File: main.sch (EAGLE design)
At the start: 23 parts, among them IC1 SN754410, IC2 7805T, T1 BP103, T2 BP103, T3 BP103

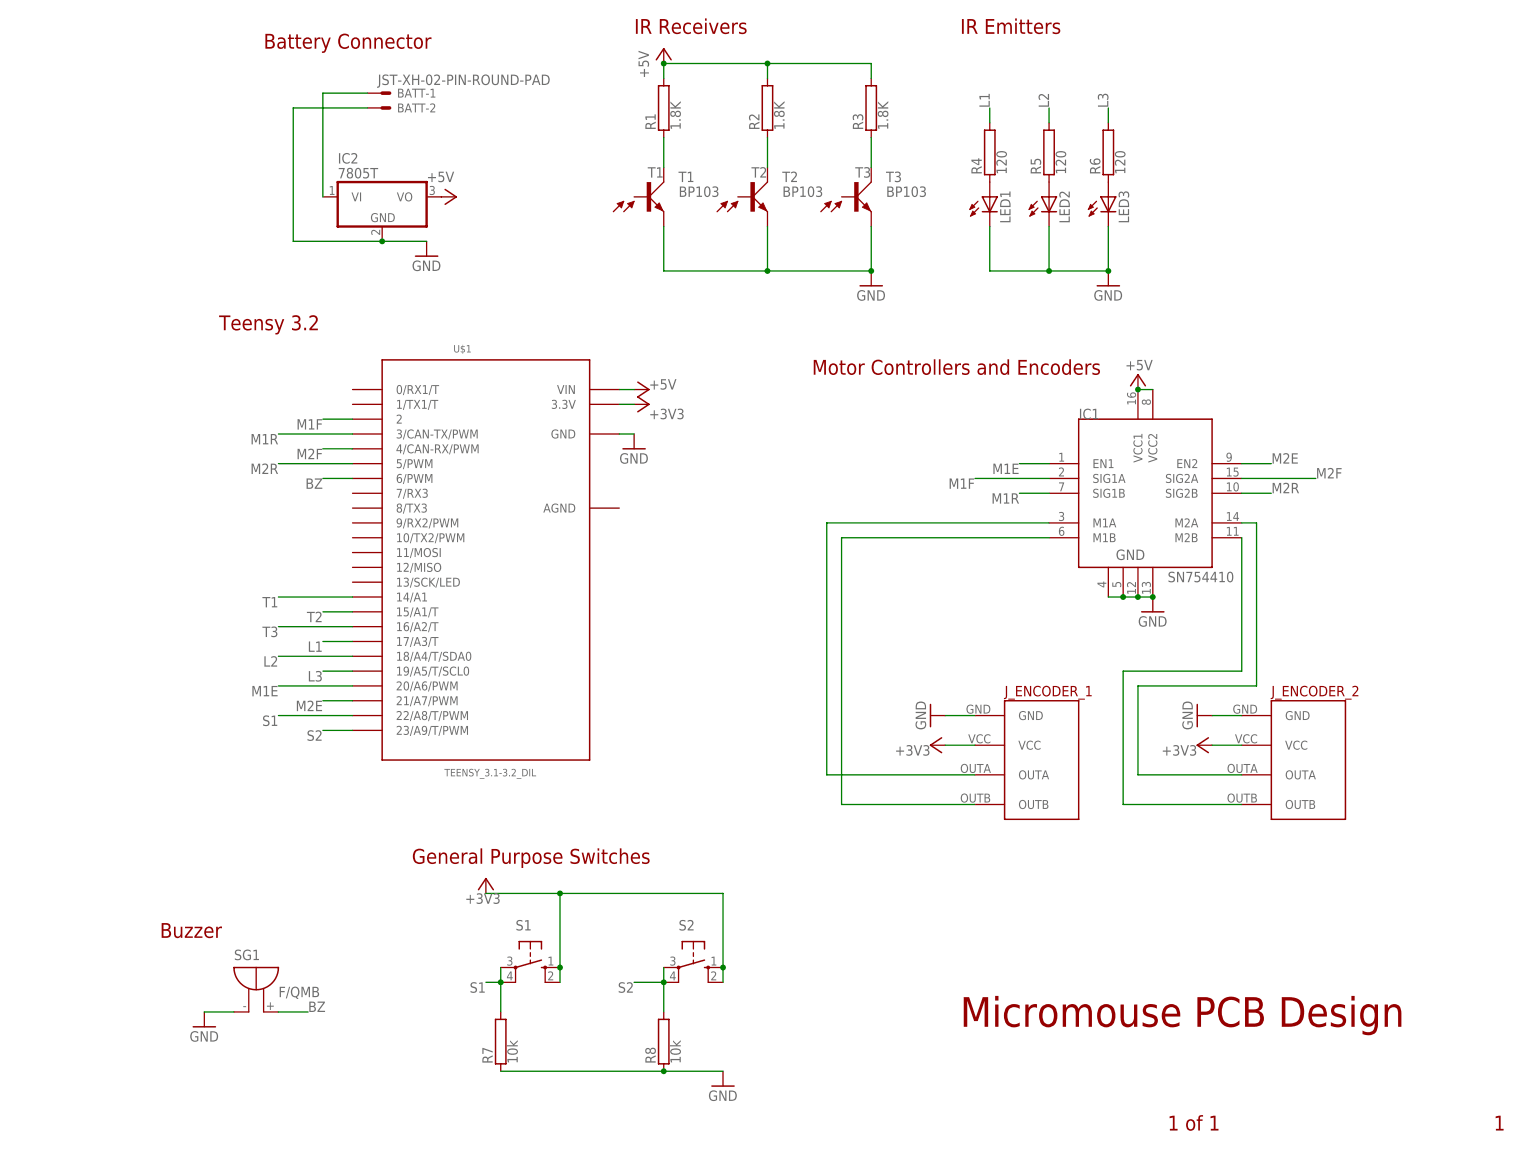
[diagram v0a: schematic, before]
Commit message: Added fourth LED/Emitter Combo and rerouted nets
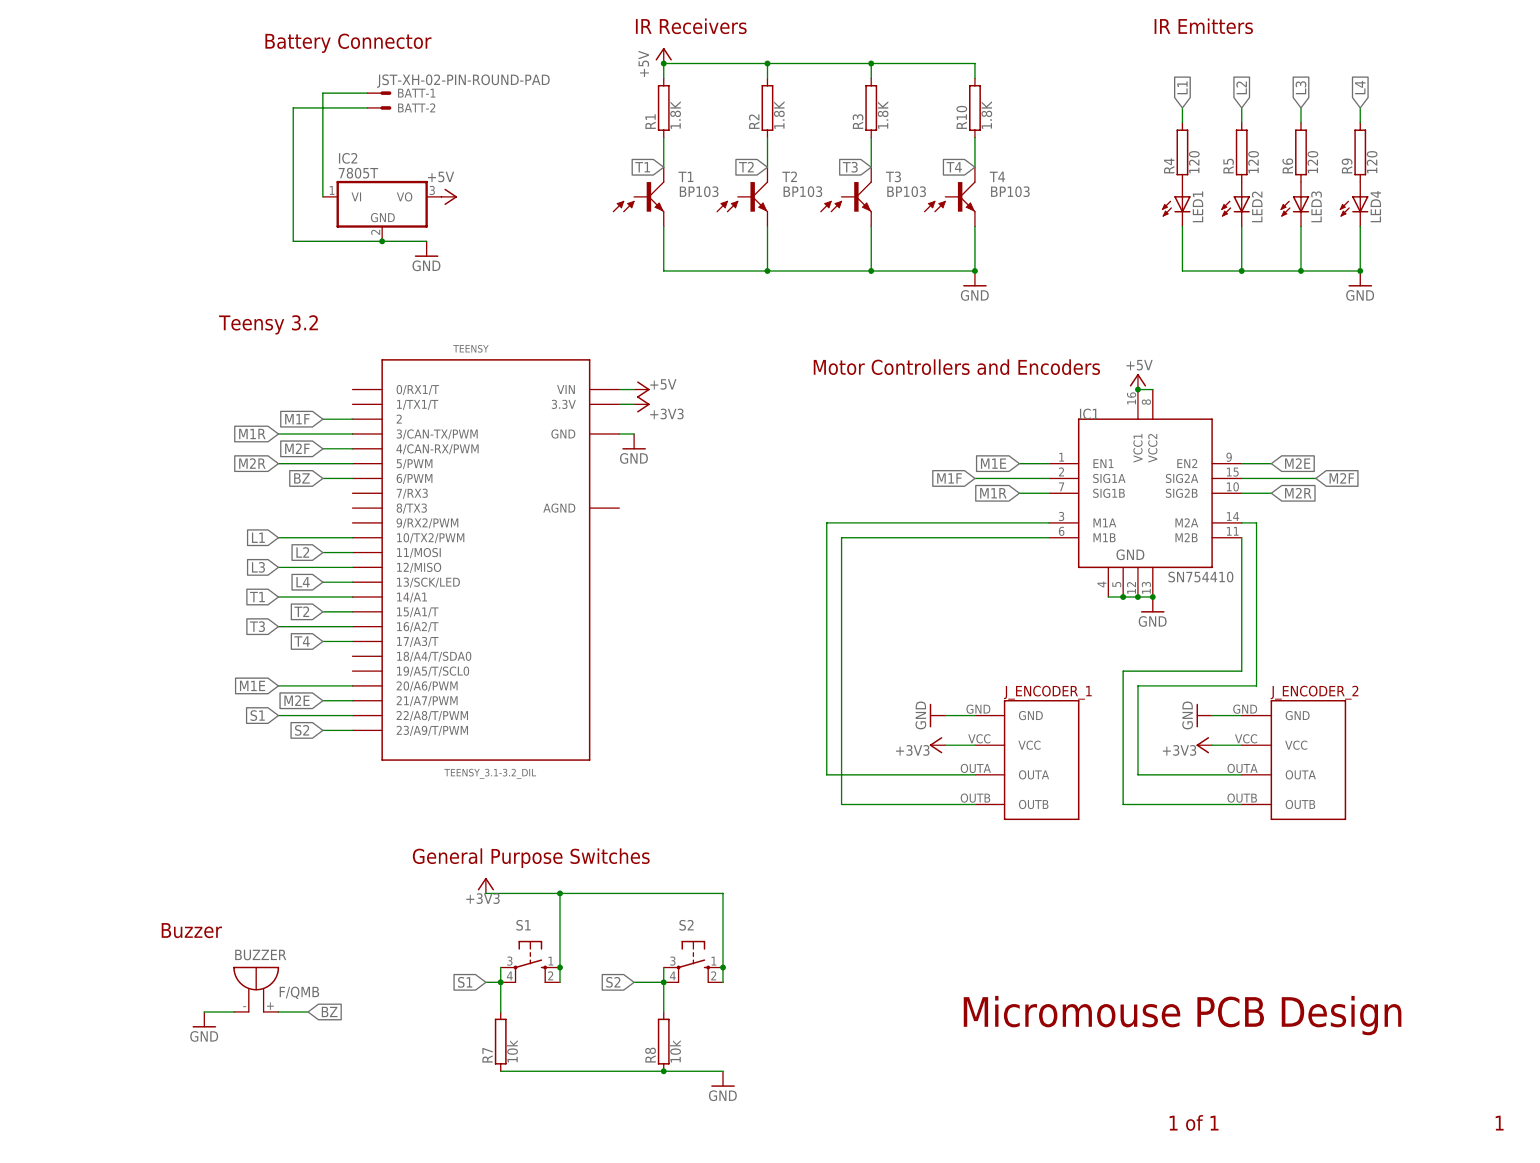
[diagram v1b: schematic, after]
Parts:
- added LED4: (no value), led:LED3MM
- added R10: 1.8K, resistor-power:RRS1/4
- added R9: 120, resistor-power:RRS1/4
- added T4: BP103, opto-trans-siemens:BP103
- renumbered SG1 to BUZZER, U$1 to TEENSY
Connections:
- new net L4: R9.2, TEENSY.13/SCK/LED
- new net N$9: LED4.A, R9.1
- new net T4: R10.1, T4.C, TEENSY.17/A3/T
- net +5V: now also R10.2
- net GND: now also LED4.C, T4.E
- net L1: now also TEENSY.10/TX2/PWM; no longer TEENSY.17/A3/T
- net L2: now also TEENSY.11/MOSI; no longer TEENSY.18/A4/T/SDA0
- net L3: now also TEENSY.12/MISO; no longer TEENSY.19/A5/T/SCL0
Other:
- moved on the sheet: LED1, LED2, LED3, R4, R5, R6

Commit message: Changed Teensy 3.2 to Teensy 2.0
Also changed switches to pull down on press, using pull up resistors on
teensy.
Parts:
- removed R7, R8: 10k, resistor-power:RRS1/4
- TEENSY: value TEENSY_3.1-3.2_DIL -> TEENSY; device Teensy_3_and_LC_Series_Boards_v1.4:TEENSY_3.1-3.2_DIL -> teensy:TEENSY; OC_NEWARK unknown -> (none)
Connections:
- net +3V3: no longer S1.S, S1.S1, S2.S, S2.S1, TEENSY.3.3V
- net +5V: now also TEENSY.5V; no longer TEENSY.VIN
- net BZ: now also TEENSY._B3; no longer TEENSY.6/PWM
- net GND: now also S1.S, S1.S1, S2.S, S2.S1, TEENSY._GND; no longer R7.1, R8.1, TEENSY.GND
- net L1: now also TEENSY._B0; no longer TEENSY.10/TX2/PWM
- net L2: now also TEENSY._B1; no longer TEENSY.11/MOSI
- net L3: now also TEENSY._B2; no longer TEENSY.12/MISO
- net L4: now also TEENSY._D1; no longer TEENSY.13/SCK/LED
- net M1E: now also TEENSY._B7; no longer TEENSY.20/A6/PWM
- net M1F: now also TEENSY._D2; no longer TEENSY.2
- net M1R: now also TEENSY._D3; no longer TEENSY.3/CAN-TX/PWM
- net M2E: now also TEENSY._D0; no longer TEENSY.21/A7/PWM
- net M2F: now also TEENSY._D6; no longer TEENSY.4/CAN-RX/PWM
- net M2R: now also TEENSY._D7; no longer TEENSY.5/PWM
- net S1: now also TEENSY._B4; no longer R7.2, TEENSY.22/A8/T/PWM
- net S2: now also TEENSY._B5; no longer R8.2, TEENSY.23/A9/T/PWM
- net T1: now also TEENSY._F0; no longer TEENSY.14/A1
- net T2: now also TEENSY._F1; no longer TEENSY.15/A1/T
- net T3: now also TEENSY._F4; no longer TEENSY.16/A2/T
- net T4: now also TEENSY._F5; no longer TEENSY.17/A3/T
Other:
- note added: "Teensy 2.0"
- note removed: "Teensy 3.2"

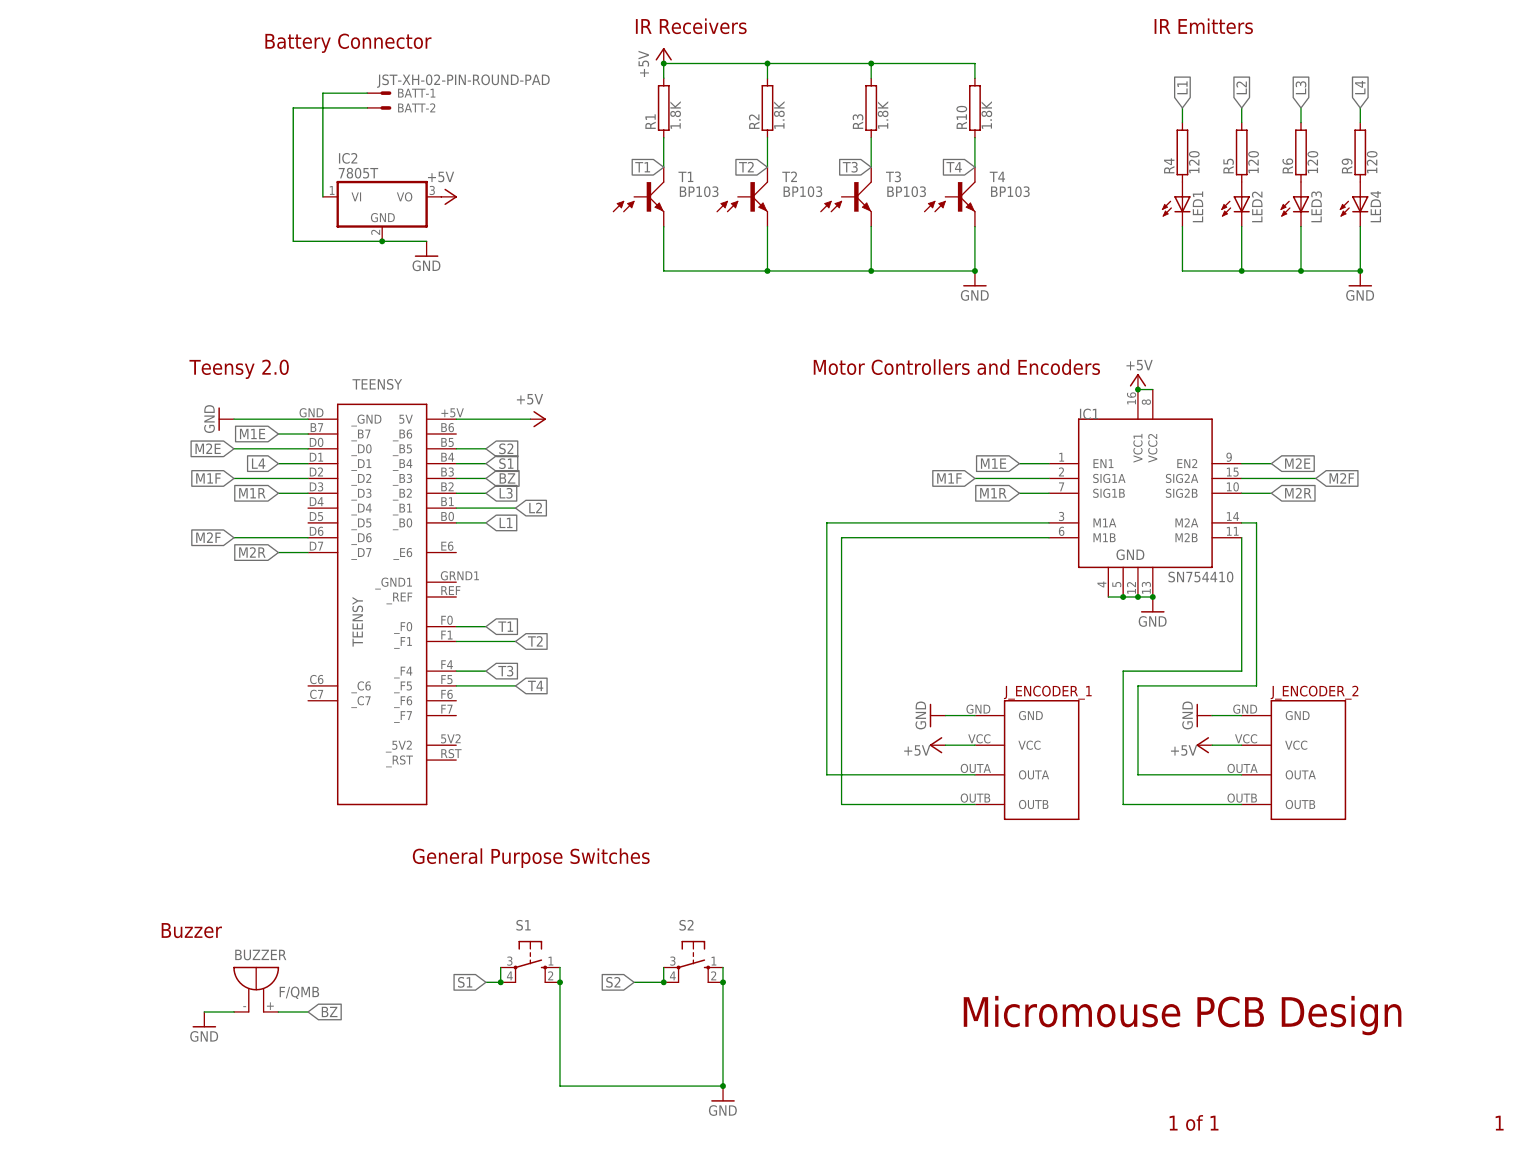
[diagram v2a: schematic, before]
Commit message: Made schematic and board consistent
Also changed transistor package
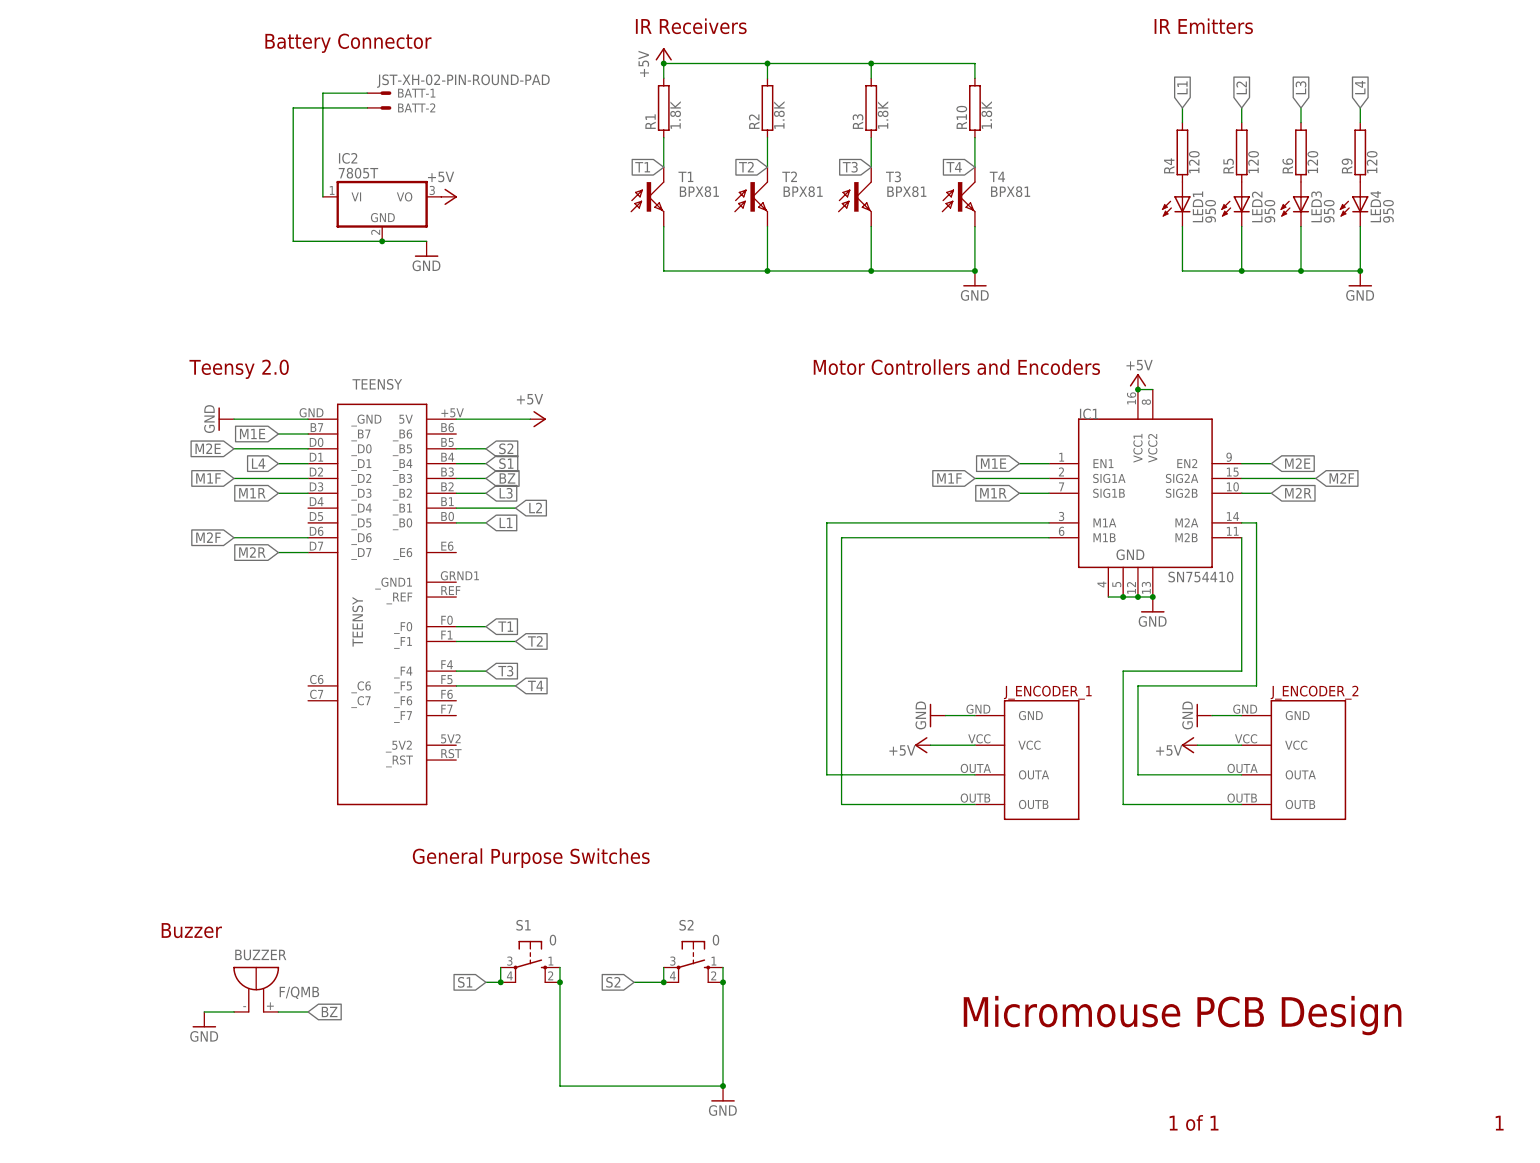
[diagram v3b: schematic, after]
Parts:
- LED1, LED2, LED3, LED4: value (none) -> 950
- S1, S2: value (none) -> 0
- T1, T2, T3, T4: value BP103 -> BPX81; device opto-trans-siemens:BP103 -> opto-trans-siemens:BPX81
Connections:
- removed net +3V3: J_ENCODER_1.VCC, J_ENCODER_2.VCC
- net +5V: now also J_ENCODER_1.VCC, J_ENCODER_2.VCC

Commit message: Update motor connection and added power switch
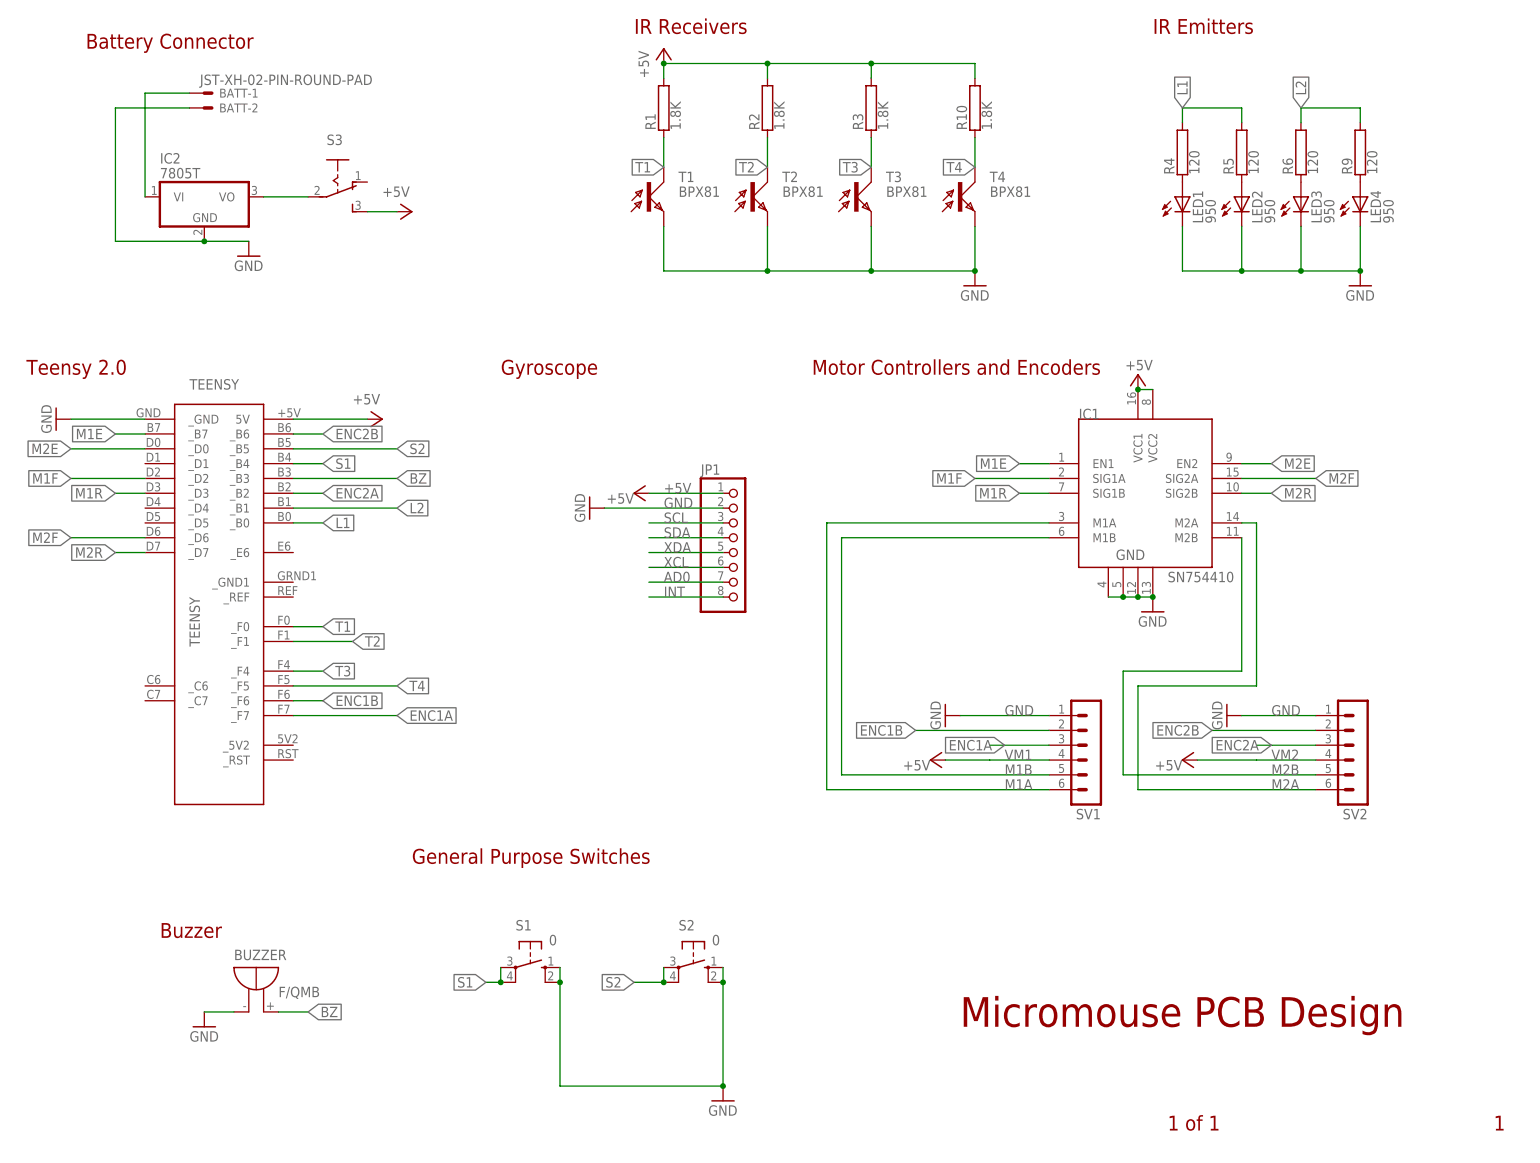
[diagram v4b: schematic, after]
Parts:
- removed J_ENCODER_1, J_ENCODER_2: ENCODER, Pololu Encoder and Motor Driver:ENCODER
- added JP1: (no value), pinhead:PINHD-1X8
- added S3: (no value), switch:255SB
- added SV1, SV2: (no value), con-lstb:MA06-1
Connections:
- removed net L3: R6.2, TEENSY._B2
- removed net L4: R9.2, TEENSY._D1
- removed net N$2: IC1.M1A, J_ENCODER_1.OUTA
- removed net N$3: IC1.M1B, J_ENCODER_1.OUTB
- removed net N$4: IC1.M2B, J_ENCODER_2.OUTB
- removed net N$5: IC1.M2A, J_ENCODER_2.OUTA
- new net AD0: JP1.7
- new net ENC1A: SV1.3, TEENSY._F7
- new net ENC1B: SV1.2, TEENSY._F6
- new net ENC2A: SV2.3, TEENSY._B2
- new net ENC2B: SV2.2, TEENSY._B6
- new net INT: JP1.8
- new net M1A: IC1.M1A, SV1.6
- new net M1B: IC1.M1B, SV1.5
- new net M2A: IC1.M2A, SV2.6
- new net M2B: IC1.M2B, SV2.5
- new net N$10: IC2.VO, S3.P
- new net SCL: JP1.3
- new net SDA: JP1.4
- new net VM1: SV1.4
- new net VM2: SV2.4
- new net XCL: JP1.6
- new net XDA: JP1.5
- net +5V: now also JP1.1, S3.S; no longer IC2.VO, J_ENCODER_1.VCC, J_ENCODER_2.VCC
- net GND: now also JP1.2, SV1.1, SV2.1; no longer J_ENCODER_1.GND, J_ENCODER_2.GND
- net L1: now also R5.2
- net L2: now also R6.2, R9.2; no longer R5.2
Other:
- note added: "Gyroscope"
- moved on the sheet: BATT-1, BATT-2, IC2, TEENSY
